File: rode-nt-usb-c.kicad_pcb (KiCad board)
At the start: 2 copper layers, 36 x 15 mm, 5 parts, among them J1 USB_C_Receptacle, J2 Conn_01x05_Pin

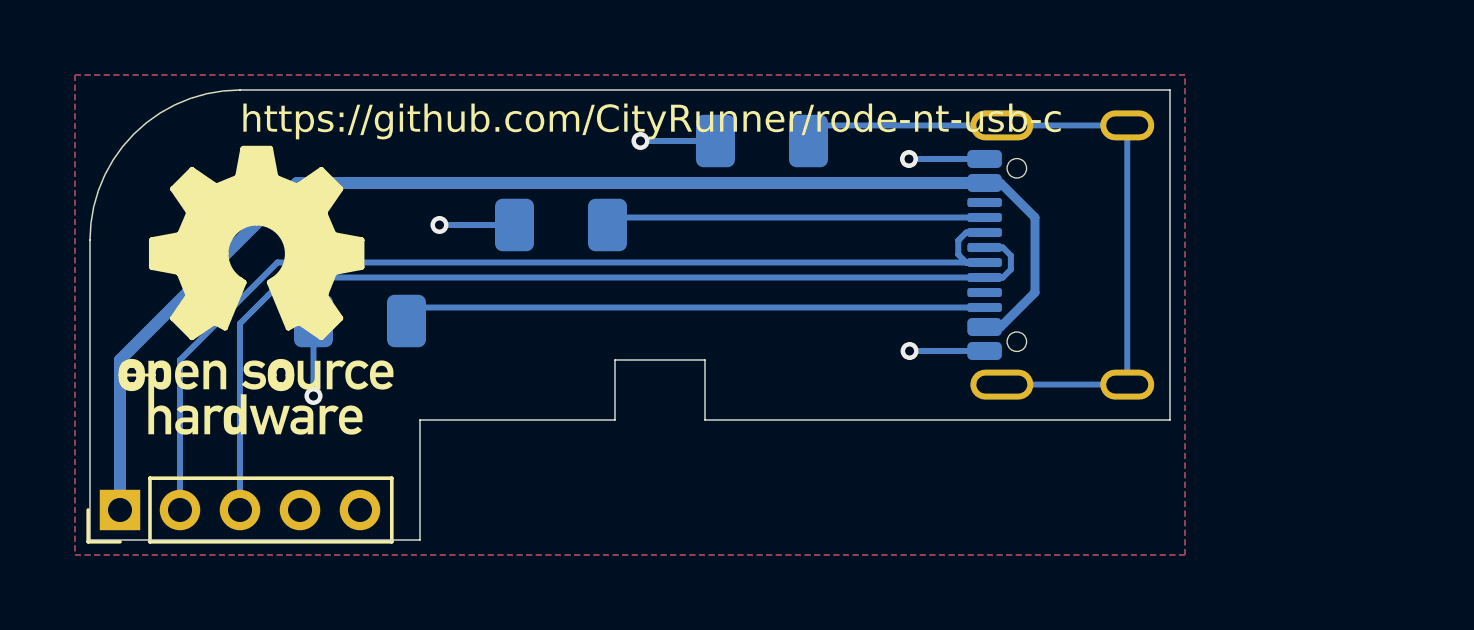
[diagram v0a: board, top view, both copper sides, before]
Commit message: Mod pcb for plastic insert
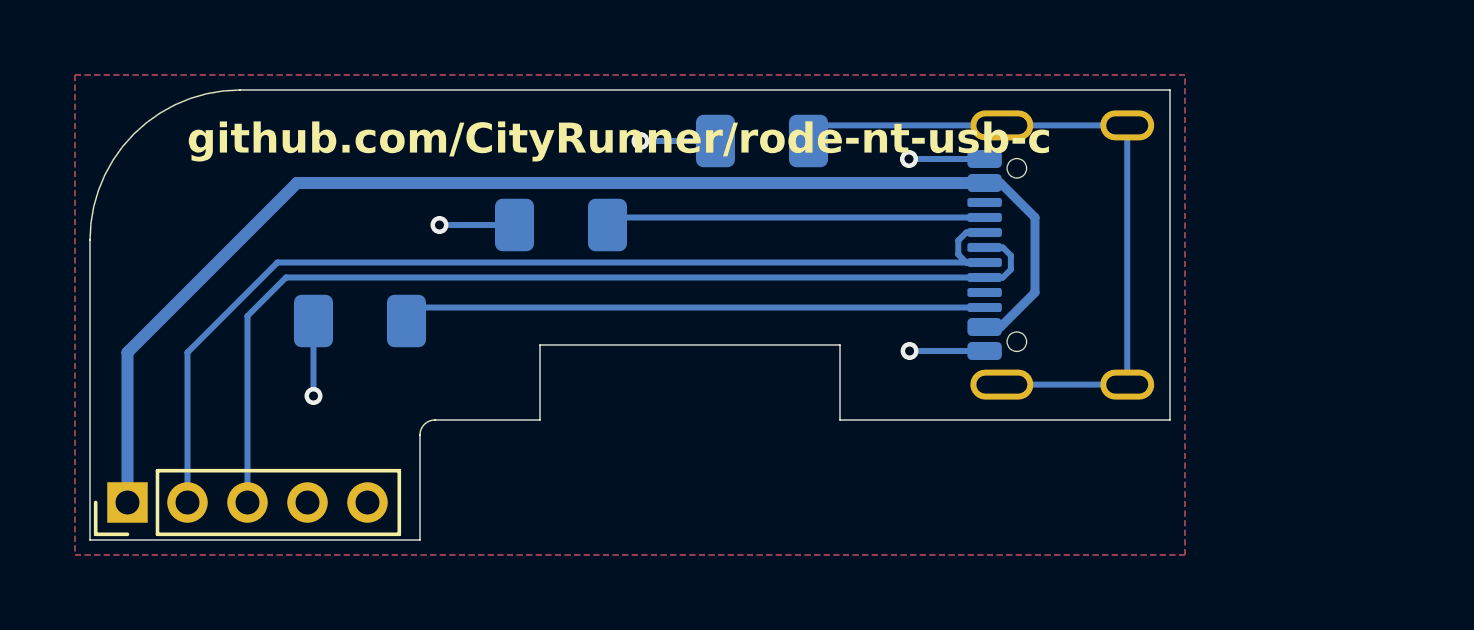
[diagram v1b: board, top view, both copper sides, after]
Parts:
- moved J2 0.35 mm to (77.2, 67.2)
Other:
- outline, holes or cut-outs redrawn
- board text added: "github.com/CityRunner/rode-nt-usb-c"
- board text removed: "https://github.com/CityRunner/rode-nt-usb-c"

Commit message: Change cutouts
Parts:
- moved J1 0.33 mm to (109.8, 59.0)
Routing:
- net +5V: track 43.3 -> 0.00 mm
- added copper zone on B.Cu, net +5V
- removed copper zone on B.Cu, net (none)
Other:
- outline, holes or cut-outs redrawn

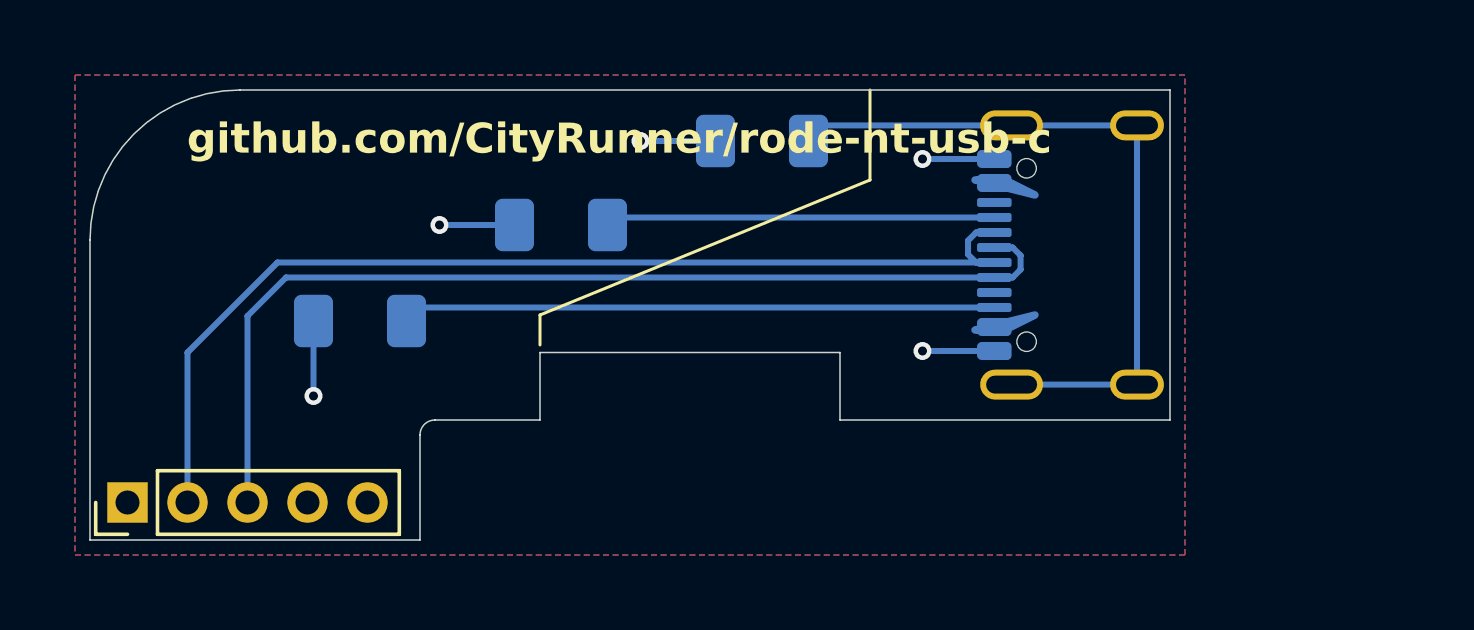
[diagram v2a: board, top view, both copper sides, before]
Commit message: Add LED, reroute
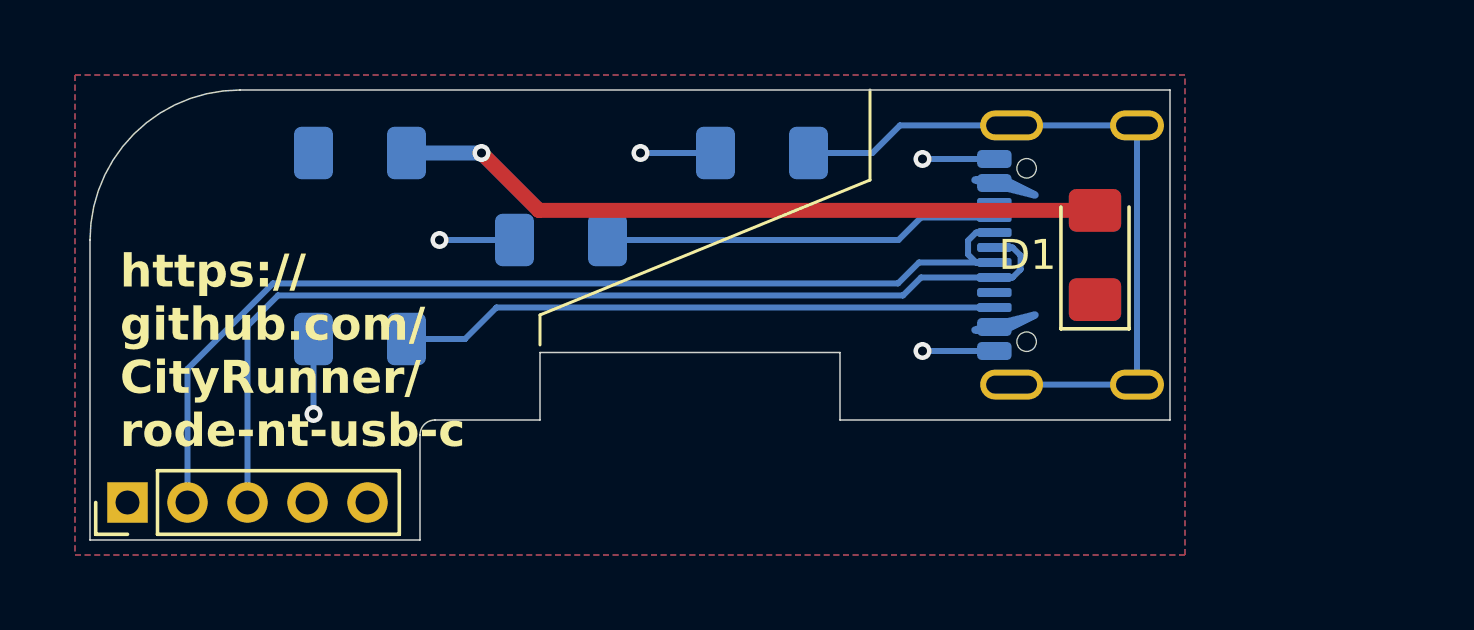
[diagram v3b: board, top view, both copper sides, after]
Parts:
- added D1: LED, LED_SMD:LED_1206_3216Metric_Pad1.42x1.75mm_HandSolder, F.Cu at (109.5, 59.0)
- added R4: R, Resistor_SMD:R_1206_3216Metric_Pad1.30x1.75mm_HandSolder, B.Cu at (85.0, 55.6)
- moved R3 0.60 mm to (85.0, 61.8)
- moved R2 0.50 mm to (91.7, 58.5)
- moved R1 0.40 mm to (98.4, 55.6)
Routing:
- net Net-(D1-A): track 0.00 -> 23.7 mm, vias 0 -> 1
- net Net-(J1-SHIELD): track 23.3 -> 24.2 mm
- net Net-(J1-CC2): track 19.1 -> 20.0 mm
- net Net-(J1-CC1): track 12.6 -> 13.2 mm
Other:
- board text added: "https:// github.com/ CityRunner/ rode-nt-usb-c"
- board text removed: "github.com/CityRunner/rode-nt-usb-c"

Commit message: Change usb side
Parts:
- removed J1: USB_C_Receptacle, Connector_USB:USB_C_Receptacle_GCT_USB4105-xx-A_16P_TopMnt_Horizontal
- added J3: USB_C_Receptacle_USB2.0_16P, Connector_USB:USB_C_Receptacle_GCT_USB4105-xx-A_16P_TopMnt_Horizontal, F.Cu at (109.8, 59.0)
- D1: moved to B.Cu
- moved R2 7.47 mm to (85.0, 61.8)
- moved R4 7.30 mm to (91.7, 58.5)
- moved R3 6.20 mm to (85.0, 55.6)
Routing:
- net Net-(D1-A): track 23.7 -> 16.7 mm, vias 1 -> 0
- net Net-(J3-CC1): track 13.2 -> 20.2 mm, vias 0 -> 1
- net D+: track 33.7 -> 30.6 mm, vias 0 -> 1
- net D-: track 35.0 -> 32.4 mm, vias 0 -> 1
- net +5V: track 0.00 -> 0.51 mm, vias 0 -> 2
- net Net-(J3-CC2): track 20.0 -> 20.3 mm, vias 0 -> 1
- net GND: track 12.3 -> 12.1 mm, vias 5 -> 4
- added copper zone on F.Cu, net +5V

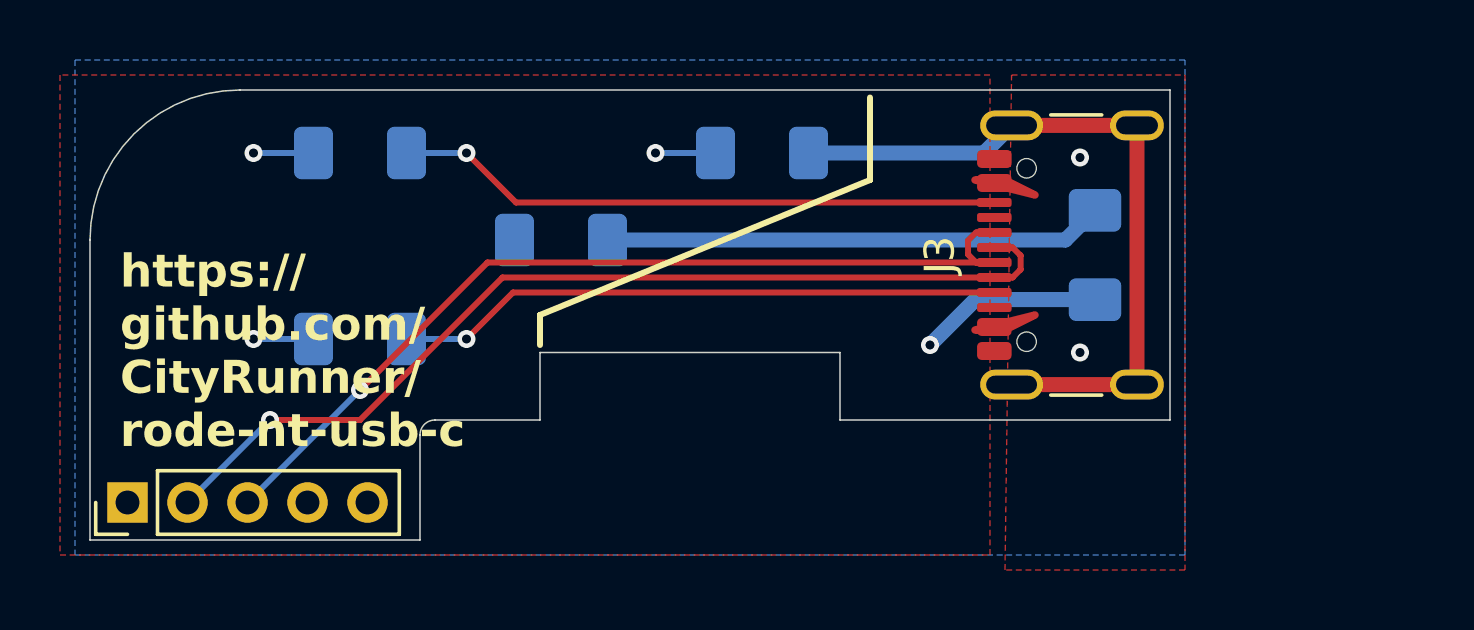
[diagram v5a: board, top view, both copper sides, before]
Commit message: Add 3d insert model, change pcb
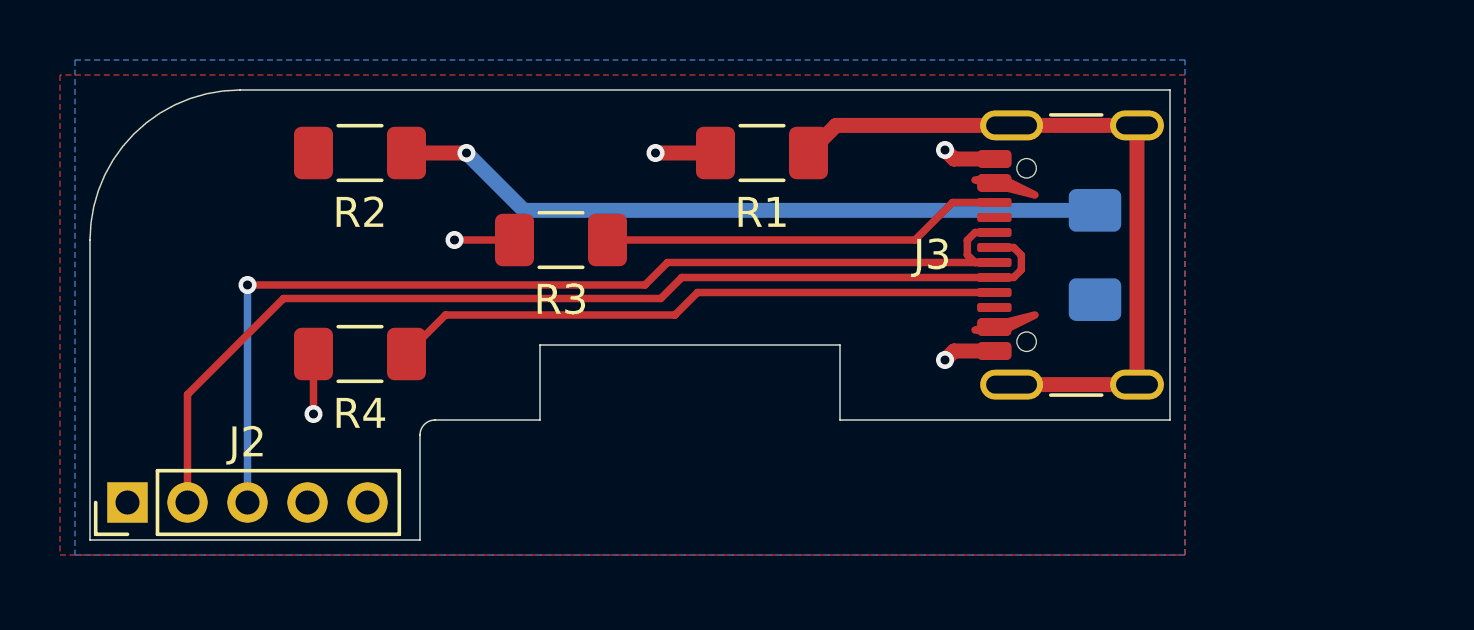
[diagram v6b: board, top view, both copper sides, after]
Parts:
- R1, R3: moved to F.Cu
- R2: renamed from R4; moved to F.Cu
- R4: renamed from R2; moved to F.Cu
- moved R2 7.30 mm to (85.0, 55.6)
- moved R3 7.30 mm to (91.7, 58.5)
- moved R4 0.50 mm to (85.0, 62.3)
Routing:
- net Net-(D1-A): track 16.7 -> 23.7 mm, vias 0 -> 1
- net Net-(J3-CC2): track 20.3 -> 13.4 mm, vias 1 -> 0
- net D+: track 30.6 -> 35.0 mm
- net GND: track 12.1 -> 9.54 mm, vias 4 -> 5
- net D-: track 32.4 -> 34.6 mm, vias 1 -> 0
- net +5V: track 0.51 -> 0.25 mm, vias 2 -> 0
- net Net-(J3-CC1): track 20.2 -> 20.4 mm, vias 1 -> 0
- added copper zone on B.Cu, net GND
- removed copper zone on B.Cu, net +5V
- removed copper zone on F.Cu, net GND
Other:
- outline, holes or cut-outs redrawn
- board text added: "https://github.com/CityRunner/rode-nt-usb-c"
- board text removed: "https:// github.com/ CityRunner/ rode-nt-usb-c"
